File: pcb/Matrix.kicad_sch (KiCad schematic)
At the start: 100 parts

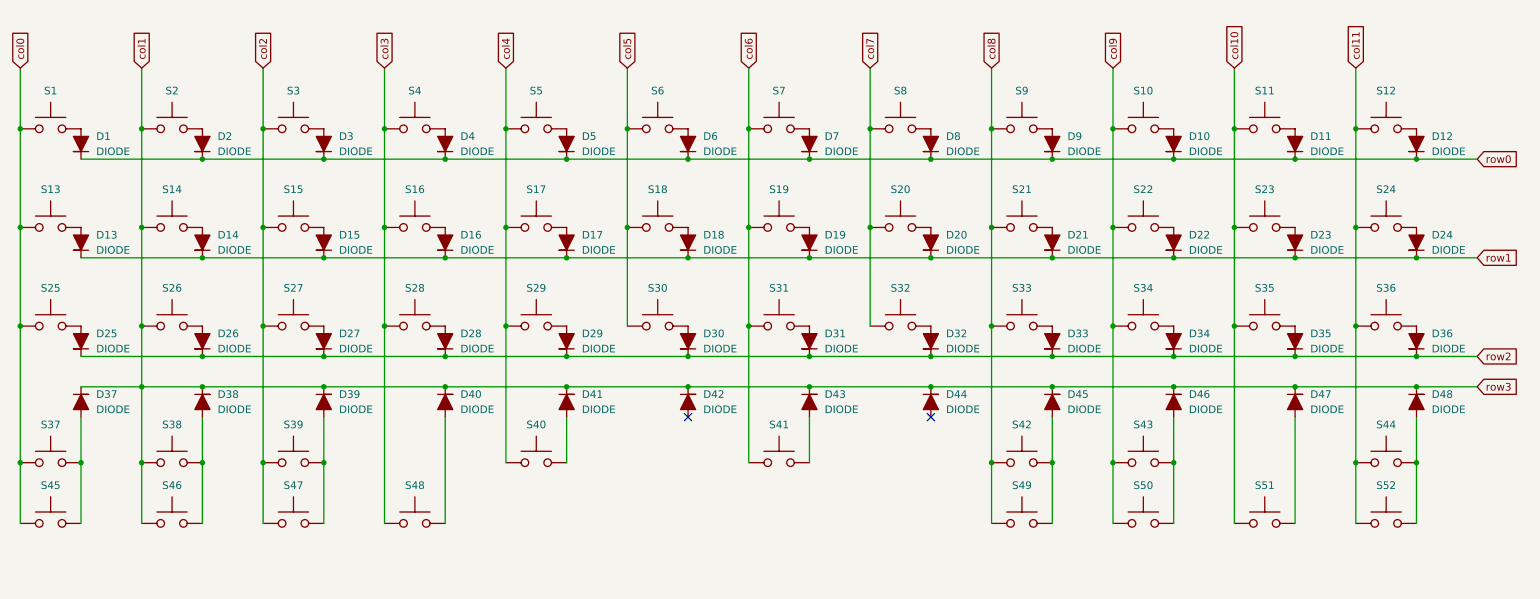
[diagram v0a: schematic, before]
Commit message: 🚧 Fixing diodes footprints issue
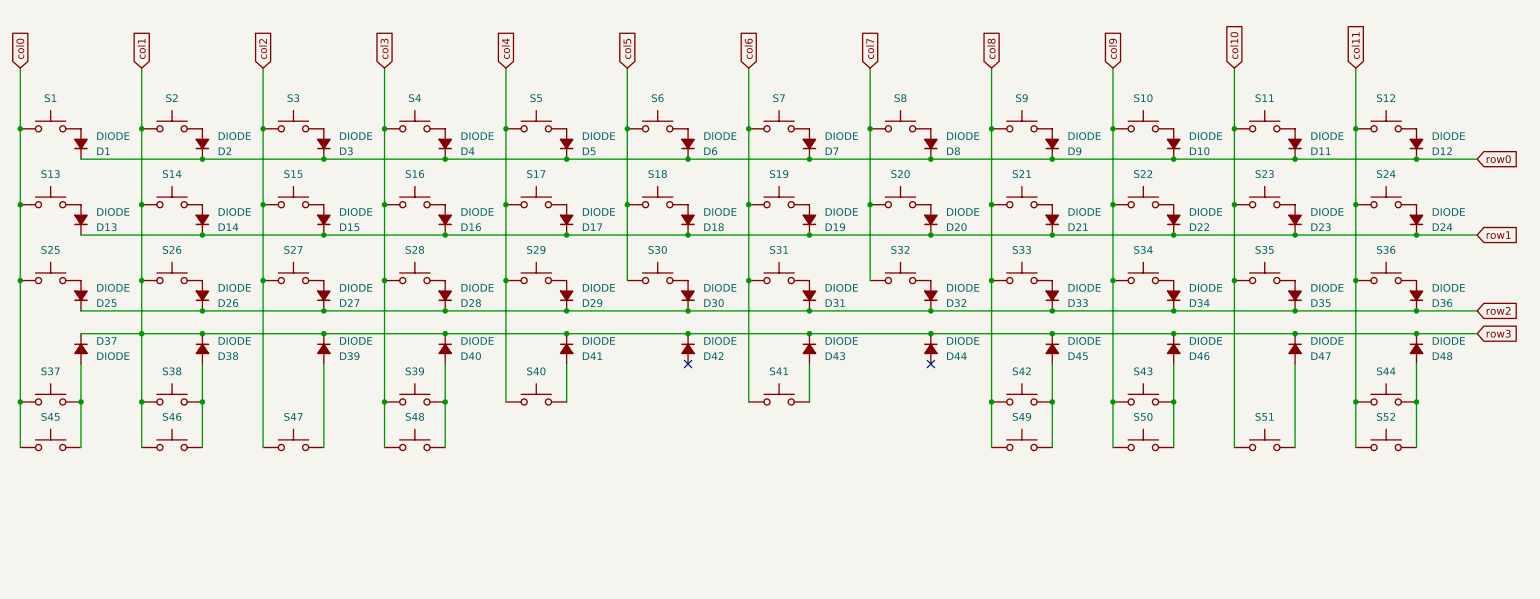
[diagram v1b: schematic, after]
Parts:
- removed D37: DIODE, Diode_THT:D_DO-35_SOD27_P7.62mm_Horizontal, symbol ElsassKabel:DIODE
- added D37: DIODE, Diode_THT:D_DO-35_SOD27_P7.62mm_Horizontal, symbol Device:D_Small_Filled
- D1, D10, D11, D12, D13, D14, D15, D16, D17, D18, D19, D2, D20, D21, D22, D23, D24, D25, D26, D27, D28, D29, D3, D30, D31, D32, D33, D34, D35, D36, D38, D39, D4, D40, D41, D42, D43, D44, D45, D46, D47, D48, D5, D6, D7, D8, D9: symbol ElsassKabel:DIODE -> Device:D_Small_Filled
- S1, S10, S11, S12, S13, S14, S15, S16, S17, S18, S19, S2, S20, S21, S22, S23, S24, S25, S26, S27, S28, S29, S3, S30, S31, S32, S33, S34, S35, S36, S37, S38, S39, S4, S40, S41, S42, S43, S44, S45, S46, S47, S48, S49, S5, S50, S51, S52, S6, S7, S8, S9: symbol ElsassKabel:SWITCH_2PIN -> Switch:SW_Push
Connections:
- net col1: now also D38.1 (K), D39.1 (K), D40.1 (K), D41.1 (K), D42.1 (K), D43.1 (K), D44.1 (K), D45.1 (K), D46.1 (K), D47.1 (K), D48.1 (K), D37.1 (K); no longer D38.2, D39.2, D40.2, D41.2, D42.2, D43.2, D44.2, D45.2, D46.2, D47.2, D48.2
- net col2: no longer S39.1
- net col3: now also S39.1
- net row0: now also D1.1 (K), D10.1 (K), D11.1 (K), D12.1 (K), D2.1 (K), D3.1 (K), D4.1 (K), D5.1 (K), D6.1 (K), D7.1 (K), D8.1 (K), D9.1 (K); no longer D1.2, D10.2, D11.2, D12.2, D2.2, D3.2, D4.2, D5.2, D6.2, D7.2, D8.2, D9.2
- net row1: now also D13.1 (K), D14.1 (K), D15.1 (K), D16.1 (K), D17.1 (K), D18.1 (K), D19.1 (K), D20.1 (K), D21.1 (K), D22.1 (K), D23.1 (K), D24.1 (K); no longer D13.2, D14.2, D15.2, D16.2, D17.2, D18.2, D19.2, D20.2, D21.2, D22.2, D23.2, D24.2
- net row2: now also D25.1 (K), D26.1 (K), D27.1 (K), D28.1 (K), D29.1 (K), D30.1 (K), D31.1 (K), D32.1 (K), D33.1 (K), D34.1 (K), D35.1 (K), D36.1 (K); no longer D25.2, D26.2, D27.2, D28.2, D29.2, D30.2, D31.2, D32.2, D33.2, D34.2, D35.2, D36.2
- net at S22.2: now also D22.2 (A); no longer D22.1
- net at S16.2: now also D16.2 (A); no longer D16.1
- net at S31.2: now also D31.2 (A); no longer D31.1
- net at S6.2: now also D6.2 (A); no longer D6.1
- net at S29.2: now also D29.2 (A); no longer D29.1
- net at S25.2: now also D25.2 (A); no longer D25.1
- net at S51.2: now also D47.2 (A); no longer D47.1
- net at S44.2, S52.2: now also D48.2 (A); no longer D48.1
- net at S9.2: now also D9.2 (A); no longer D9.1
- net at S23.2: now also D23.2 (A); no longer D23.1
- net at S17.2: now also D17.2 (A); no longer D17.1
- net at S48.2: now also D40.2 (A), S39.2; no longer D40.1
- net at S13.2: now also D13.2 (A); no longer D13.1
- net at S5.2: now also D5.2 (A); no longer D5.1
- net at S34.2: now also D34.2 (A); no longer D34.1
- net at S24.2: now also D24.2 (A); no longer D24.1
- net at S1.2: now also D1.2 (A); no longer D1.1
- net at S14.2: now also D14.2 (A); no longer D14.1
- net at S43.2, S50.2: now also D46.2 (A); no longer D46.1
- net at S3.2: now also D3.2 (A); no longer D3.1
- net at S7.2: now also D7.2 (A); no longer D7.1
- net at S12.2: now also D12.2 (A); no longer D12.1
- net at S28.2: now also D28.2 (A); no longer D28.1
- net at S21.2: now also D21.2 (A); no longer D21.1
- net at S35.2: now also D35.2 (A); no longer D35.1
- net at S2.2: now also D2.2 (A); no longer D2.1
- net at S8.2: now also D8.2 (A); no longer D8.1
- net at S41.2: now also D43.2 (A); no longer D43.1
- net at S18.2: now also D18.2 (A); no longer D18.1
- net at S10.2: now also D10.2 (A); no longer D10.1
- net at S19.2: now also D19.2 (A); no longer D19.1
- net at S37.2, S45.2: now also D37.2 (A)
- net at S42.2, S49.2: now also D45.2 (A); no longer D45.1
- net at S33.2: now also D33.2 (A); no longer D33.1
- net at S30.2: now also D30.2 (A); no longer D30.1
- net at S11.2: now also D11.2 (A); no longer D11.1
- net at S38.2, S46.2: now also D38.2 (A); no longer D38.1
- net at S27.2: now also D27.2 (A); no longer D27.1
- net at S36.2: now also D36.2 (A); no longer D36.1
- net at S26.2: now also D26.2 (A); no longer D26.1
- net at S20.2: now also D20.2 (A); no longer D20.1
- net at S4.2: now also D4.2 (A); no longer D4.1
- net at S40.2: now also D41.2 (A); no longer D41.1
- net at S15.2: now also D15.2 (A); no longer D15.1
- net at S32.2: now also D32.2 (A); no longer D32.1
- new net: D39.2 (A), S47.2
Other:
- moved on the sheet: S1, S10, S11, S12, S13, S14, S15, S16, S17, S18, S19, S2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

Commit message: 🚧 WIP - Place the components - Wire all the components
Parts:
- added S53: SWITCH_2PIN, ElsassKabel:SW_Cherry_MX_PCB_6.25u, symbol Switch:SW_Push
- added S54, S57, S59, S61: SWITCH_2PIN, ElsassKabel:SW_Cherry_MX_PCB_1.00u, symbol Switch:SW_Push
- added S55, S58: SWITCH_2PIN, ElsassKabel:SW_Cherry_MX_PCB_1.25u, symbol Switch:SW_Push
- added S56: SWITCH_2PIN, ElsassKabel:SW_Cherry_MX_PCB_7.00u, symbol Switch:SW_Push
- added S60: SWITCH_2PIN, ElsassKabel:SW_Cherry_MX_PCB_2.25u, symbol Switch:SW_Push
- added S62: SWITCH_2PIN, ElsassKabel:SW_Cherry_MX_PCB_2.75u, symbol Switch:SW_Push
- S1, S10, S11, S14, S15, S16, S17, S18, S19, S2, S20, S21, S22, S23, S26, S27, S28, S29, S3, S30, S31, S32, S33, S34, S35, S36, S4, S45, S46, S47, S48, S5, S50, S51, S52, S6, S7, S8, S9: footprint Switch_Keyboard_Cherry_MX:SW_Cherry_MX_PCB_1.00u -> ElsassKabel:SW_Cherry_MX_PCB_1.00u
- S12, S25, S44: footprint Switch_Keyboard_Cherry_MX:SW_Cherry_MX_PCB_1.75u -> ElsassKabel:SW_Cherry_MX_PCB_1.75u
- S13, S37, S39, S42: footprint Switch_Keyboard_Cherry_MX:SW_Cherry_MX_PCB_1.25u -> ElsassKabel:SW_Cherry_MX_PCB_1.25u
- S24, S38, S43, S49: footprint Switch_Keyboard_Cherry_MX:SW_Cherry_MX_PCB_1.50u -> ElsassKabel:SW_Cherry_MX_PCB_1.50u
- S40: footprint Switch_Keyboard_Cherry_MX:SW_Cherry_MX_PCB_2.25u -> ElsassKabel:SW_Cherry_MX_PCB_2.25u
- S41: footprint Switch_Keyboard_Cherry_MX:SW_Cherry_MX_PCB_2.00u -> ElsassKabel:SW_Cherry_MX_PCB_2.00u
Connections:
- net col0: now also S57.1
- net col1: now also S54.1, S58.1; no longer D37.1 (K), D38.1 (K), D39.1 (K), D40.1 (K), D41.1 (K), D42.1 (K), D43.1 (K), D44.1 (K), D45.1 (K), D46.1 (K), D47.1 (K), D48.1 (K)
- net col2: now also S55.1, S59.1
- net col4: now also S60.1
- net col5: now also S53.1, S56.1, S61.1
- net col7: now also S62.1
- net at D39.2 (A), S47.2: now also S55.2, S59.2
- net at D37.2 (A), S37.2, S45.2: now also S57.2
- net at D38.2 (A), S38.2, S46.2: now also S54.2, S58.2
- net at D41.2 (A), S40.2: now also S60.2
- net at D44.2 (A): now also S62.2
- net at D42.2 (A): now also S53.2, S56.2, S61.2
- new net row3: D37.1 (K), D38.1 (K), D39.1 (K), D40.1 (K), D41.1 (K), D42.1 (K), D43.1 (K), D44.1 (K), D45.1 (K), D46.1 (K), D47.1 (K), D48.1 (K)
- no-connect marks 2 -> 0

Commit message: 🏗️ Prepare for production
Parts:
- added S63, S64, S65: SWITCH_2PIN, ElsassKabel:SW_Cherry_MX_PCB_1.25u, symbol Switch:SW_Push
- added S66: SWITCH_2PIN, ElsassKabel:SW_Cherry_MX_PCB_6.25u, symbol Switch:SW_Push
- S57: footprint ElsassKabel:SW_Cherry_MX_PCB_1.00u -> ElsassKabel:SW_Cherry_MX_PCB_1.25u
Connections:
- net col0: no longer S57.1
- net col1: now also S57.1
- net col10: now also S64.1
- net col2: now also S65.1
- net col5: now also S66.1
- net col9: now also S63.1
- net at D38.2 (A), S38.2, S46.2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: now also S57.2
- net at D47.2 (A), S51.2: now also S64.2
- net at D46.2 (A), S43.2, S50.2: now also S63.2
- net at D39.2 (A), S47.2, S55.2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: now also S65.2
- net at D42.2 (A), S53.2, S56.2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: now also S66.2
- net at D37.2 (A), S37.2, S45.2: no longer S57.2
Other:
- title: EK_Van -> RetroVan
- moved on the sheet: S47, S51, S53, S55, S56, S57, S58, S59, S60, S61, S62
